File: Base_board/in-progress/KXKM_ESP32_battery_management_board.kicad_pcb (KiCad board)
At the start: 4 copper layers, 56.5 x 57.5 mm, 109 parts, among them J1 Conn_01x06, J11 TEST_1P, J13 Wire pad, J14 Wire pad, J15 Wire pad, J16 Wire pad, J2 TEST_1P, J3 Conn_02x10_Odd_Even, J4 Conn_01x04, J5 Conn_01x02, J6 Conn_01x03, J7 Conn_01x03, J8 Conn_01x03, J9 USB_A, P1 TC_SWD, Q1 BC847W, Q2 BC847W, Q4 2N7002, Q5 2N7002, Q6 2N7002, SW1 SW_Push, SW2 SW_DIP_x03, SW3 SW_Push, SW4 SW_SP3T, U1 ESP32-WROOM, U2 SP3485CN, U3 MCP16331T-E/CH, U4 BTS50080-1TEA, U5 DC_DC_POL, U7 STM32F030F4Px

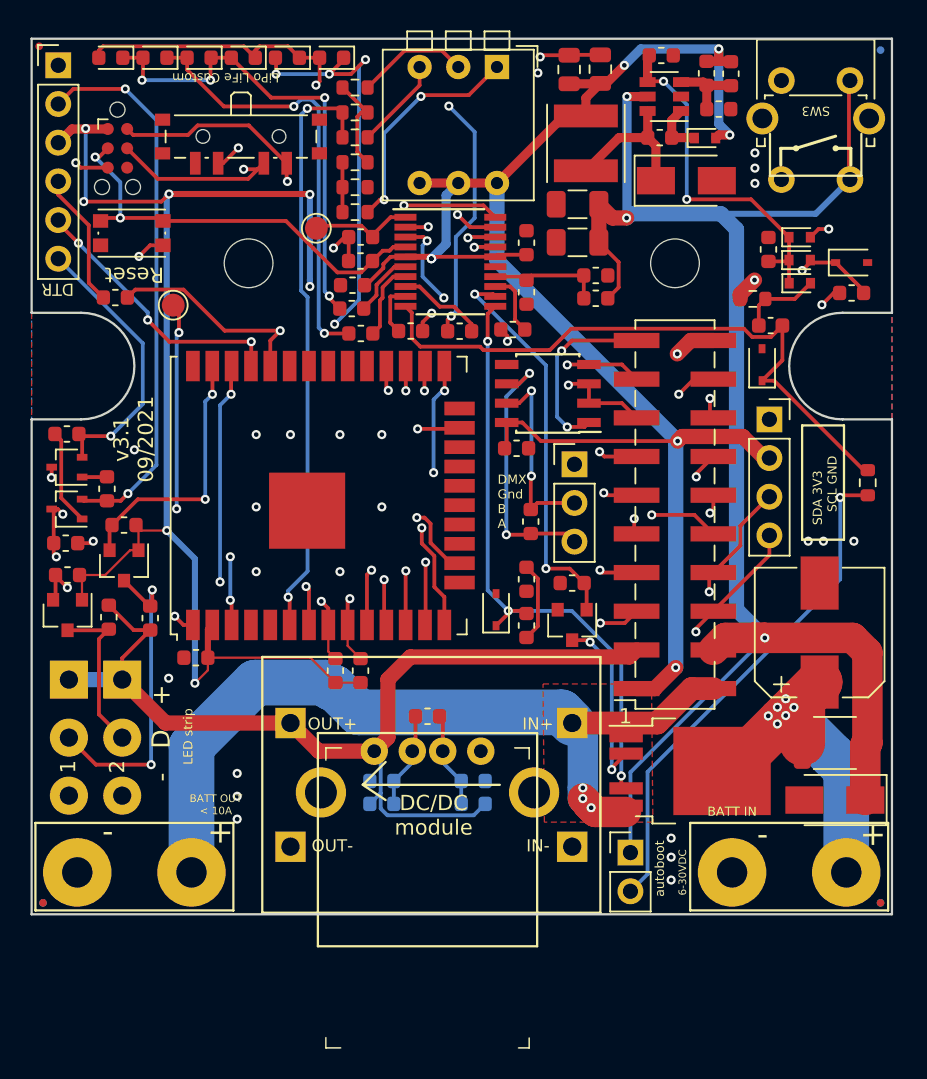
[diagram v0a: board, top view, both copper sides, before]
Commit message: update v3.2
-  connecteur XT60 coudé (et disponible chez JLCPCB)
- modification de l’autoboot pour un redémarrage en cas de perte brêve d’alimentation,
- ajout de l’empreinte pour rajouter une lecteur microSD
- mise à jour des piste de sortie batterie conforme pour 10A
- suppression des pin I2C (déjà dispo sur le GPIO)
- connecteur JST B3B-EH pour un câblage et éviter les soudure qui casse sur les sortie pour LED
- ESP32 en version 16M
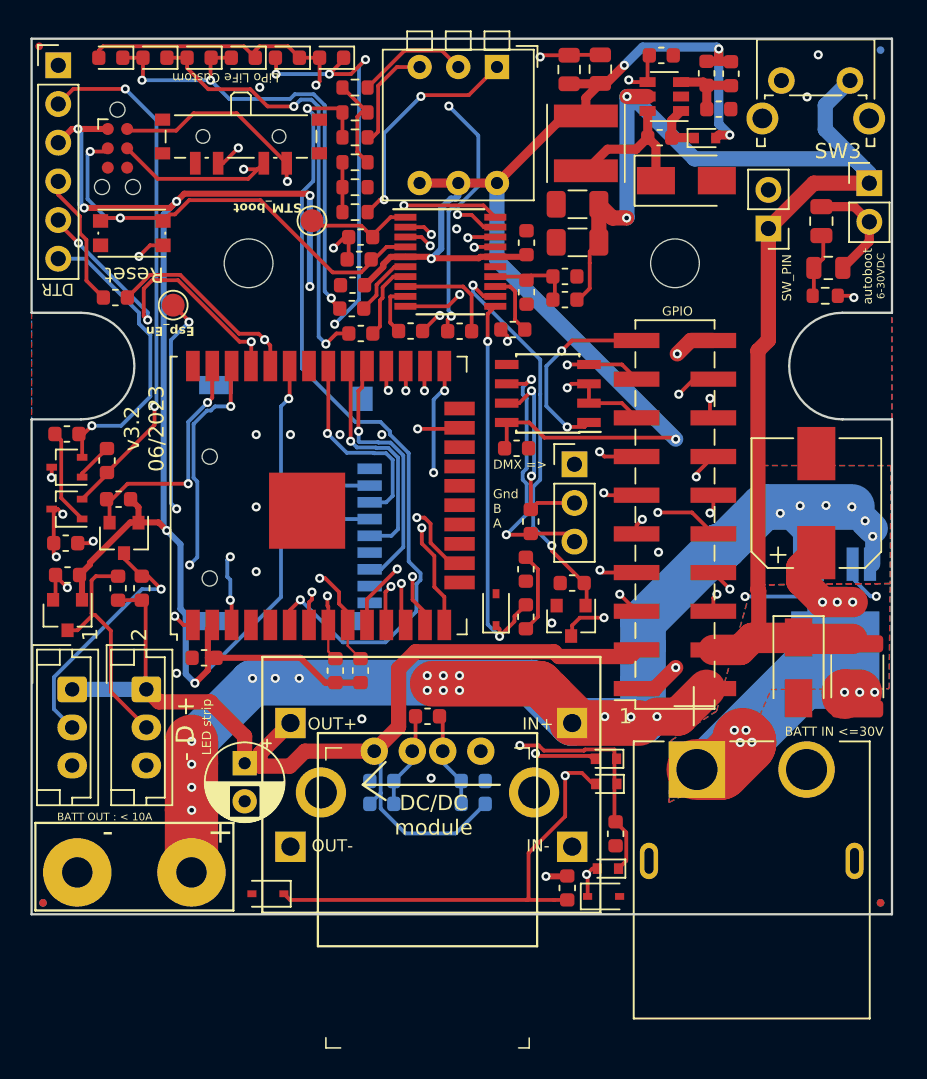
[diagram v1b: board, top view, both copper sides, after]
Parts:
- removed J13, J14: Wire pad, Connector_Wire:SolderWirePad_1x01_Drill2mm
- removed R32: 47k, Resistor_SMD:R_0603_1608Metric
- added C12: 10uF, Capacitor_SMD:C_0805_2012Metric, F.Cu at (154.9, 92.5)
- added C13: 220uF, Capacitor_THT:CP_Radial_D5.0mm_P2.50mm, F.Cu at (117.0, 128.1)
- added J10: XT60PW-M, XT60PW-M:AMASS_XT60PW-M, F.Cu at (150.3, 134.5)
- added J12: Conn_01x02_Socket, Connector_PinHeader_2.54mm:PinHeader_1x02_P2.54mm_Vertical, F.Cu at (151.4, 93.0)
- C11: value 1uF -> 10uF; footprint Capacitor_SMD:C_0603_1608Metric -> Capacitor_SMD:C_0805_2012Metric
- J4: value Conn_01x04 -> 112J-TDAR-R01; footprint Connector_PinSocket_2.54mm:PinSocket_1x04_P2.54mm_Vertical -> KiCad:112JTDARR01; moved to B.Cu
- J7, J8: footprint tom_kicad_lib:SolderWirePad_1x03_P3.81mm_Drill1.2mm -> Connector_JST:JST_EH_B3B-EH-A_1x03_P2.50mm_Vertical
- SW3: footprint tom_kicad_lib:SW_Tactile_SPST_Angled_PTS645Vx58-2LFS_horiz_pads -> Button_Switch_THT:SW_Tactile_SPST_Angled_PTS645Vx31-2LFS
- U4: moved to B.Cu
- U7: value STM32F030F4Px -> STM32F070F6Px
- moved D2 56.5 mm to (118.5, 136.7), turned to 180 degrees
- moved J5 46.7 mm to (158.0, 90.0)
- moved R8 43.3 mm to (138.2, 136.3), turned to -90 degrees
- moved D15 40.5 mm to (140.8, 135.0), turned to 180 degrees
- moved R1 39.7 mm to (141.4, 132.7), turned to -90 degrees
- moved D4 36.7 mm to (140.7, 129.4), turned to 180 degrees
- moved D1 36.5 mm to (140.7, 127.8), turned to 180 degrees
- moved D14 36.4 mm to (140.6, 136.8), turned to 0 degrees
- moved J4 34.0 mm to (117.9, 111.0), turned to 90 degrees
- moved U4 13.4 mm to (155.8, 119.2), turned to -90 degrees
- moved R28 12.6 mm to (155.1, 97.4), turned to 0 degrees
- moved D11 9.00 mm to (153.4, 121.8), turned to -90 degrees
- moved C6 8.50 mm to (154.5, 111.0)
- moved C11 5.36 mm to (155.3, 95.6)
- moved F1 4.62 mm to (157.2, 122.4), turned to -90 degrees
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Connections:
- net /Battery monitoring/STM32_RESET renamed /Battery monitoring/STM32_RST
- net Net-(C26-Pad1) renamed /Power/EN
- C11 pad 1: /Battery monitoring/AUTOBOOT_SENSE -> Net-(J5-Pin_2)
- D15 pad 2: Net-(C11-Pad2) -> /Battery monitoring/AUTOBOOT_SENSE
- J4 pad 1: GND -> unconnected-(J4-DAT2-Pad1)
- J4 pad 2: +3V3 -> /SD_CS
- J4 pad 3: /I2C_SCL -> /SD_DI
- J4 pad 4: /I2C_SDA -> +3V3
- J5 pad 2: Net-(J5-Pad2) -> Net-(J5-Pin_2)
- P1 pad 6: (no net) -> unconnected-(P1-SWO-Pad6)
- R28 pad 1: Net-(J5-Pad2) -> Net-(C11-Pad2)
- SW4 pad 4: (no net) -> unconnected-(SW4-Pad4)
- U1 pad 17: (no net) -> unconnected-(U1-SD2/IO9-Pad17)
- U1 pad 18: (no net) -> unconnected-(U1-SD3/IO10-Pad18)
- U1 pad 19: (no net) -> unconnected-(U1-CMD/IO11-Pad19)
- U1 pad 20: (no net) -> unconnected-(U1-CLK/IO6-Pad20)
- U1 pad 21: (no net) -> unconnected-(U1-SD0/IO7-Pad21)
- U1 pad 22: (no net) -> unconnected-(U1-SD1/IO8-Pad22)
- U1 pad 24: (no net) -> unconnected-(U1-IO2-Pad24)
- U1 pad 29: (no net) -> /SD_DO
- U1 pad 30: (no net) -> /SD_SCK
- U1 pad 31: (no net) -> /SD_DI
- U1 pad 32: (no net) -> unconnected-(U1-NC-Pad32)
- U1 pad 33: (no net) -> /SD_CS
- U1 pad 4: (no net) -> unconnected-(U1-SENSOR_VP-Pad4)
- U1 pad 5: (no net) -> unconnected-(U1-SENSOR_VN-Pad5)
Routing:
- net +VSW: track 96.9 -> 221.3 mm, vias 3 -> 22
- net /Battery monitoring/AUTOBOOT_SENSE: track 41.6 -> 105.5 mm, vias 0 -> 3
- net /Power/EN: track 23.4 -> 80.9 mm
- net Net-(J12-Pin_2): track 20.0 -> 71.3 mm
- net /Battery monitoring/EN_PUSH_BUTTON: track 36.4 -> 71.5 mm, vias 3 -> 2
- net Net-(J5-Pad2): track 33.4 -> 0.00 mm, vias 1 -> 0
- net /Battery monitoring/LOAD_I_SENSE: track 40.7 -> 71.7 mm
- net +BATT_RAW: track 37.6 -> 58.9 mm, vias 6 -> 10
- net +BATT: track 109.0 -> 89.6 mm, vias 3 -> 2
- net /SD_DO: track 0.00 -> 17.4 mm, vias 0 -> 1
- net /SD_SCK: track 0.00 -> 15.3 mm, vias 0 -> 1
- net /Battery monitoring/3.3V_EN: track 29.3 -> 43.8 mm
- net /DIP_SWITCH: track 38.9 -> 53.4 mm
- net /SD_CS: track 0.00 -> 13.5 mm, vias 0 -> 1
- net /SD_DI: track 0.00 -> 13.5 mm, vias 0 -> 1
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- added copper zone on B.Cu, net +BATT_RAW
- added copper zone on F.Cu, net +BATT_RAW
- added copper zone on In1.Cu, net +BATT_RAW
- added copper zone on In2.Cu, net +BATT_RAW
- added copper zone on B.Cu, net +VSW
- added copper zone on In1.Cu, net +VSW
- added copper zone on In2.Cu, net +VSW
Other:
- board text added: "0"
- board text added: "0 mm"
- board text added: "0,01 mm"
- board text added: "0,02"
- board text added: "0,035 mm"
- board text added: "0,1500 mm / 0,0000 mm"
- board text added: "0,3000 mm"
- board text added: "0,48 mm"
- board text added: "1,6000 mm"
- board text added: "2 1"
- board text added: "3,3"
- board text added: "4"
- board text added: "4,5"
- board text added: "56,5000 mm x 57,5000 mm"
- board text added: "B.Cu"
- board text added: "B.Mask"
- board text added: "B.Paste"
- board text added: "B.Silkscreen"
- board text added: "BATT IN <=30V"
- board text added: "BATT OUT : < 10A"
- board text added: "BTS50080-1TEA"
- board text added: "Bottom Silk Screen"
- board text added: "Bottom Solder Mask"
- board text added: "Bottom Solder Paste"
- board text added: "C. Saillant / V. Henry / Tom Magnier v3.2 - 06/2023"
- board text added: "CARACTÉRISTIQUES du PCB"
- board text added: "Connecteurs de bord de cartes:"
- board text added: "Contour du PCB Métallisé:"
- board text added: "Contrôle d'Impédance:"
- board text added: "Couleur"
- board text added: "DMX => Gnd B A"
- board text added: "Diamètre de trou min:"
- board text added: "Dimensions hors tout PCB:"
- board text added: "Diélectrique"
- board text added: "Epaisseur du PCB:"
- board text added: "Epsilon R"
- board text added: "Esp_En"
- board text added: "F.Cu"
- board text added: "F.Mask"
- board text added: "F.Paste"
- board text added: "F.Silkscreen"
- board text added: "FR4"
- board text added: "Finition Cuivre:"
- board text added: "GPIO"
- board text added: "In1.Cu"
- board text added: "In2.Cu"
- board text added: "Matériel"
- board text added: "Micro_SD 112J-TDAR-R01"
- board text added: "Nom de Couche"
- board text added: "Nombre de Couches Cuivre:"
- board text added: "Non"
- board text added: "None"
- board text added: "Not specified"
- board text added: "Pads castellated:"
- board text added: "Piste / espacement min:"
- board text added: "STM_boot"
- board text added: "SW_PIN"
- board text added: "Tg Perte"
- board text added: "Top Silk Screen"
- board text added: "Top Solder Mask"
- board text added: "Top Solder Paste"
- board text added: "Type"
- board text added: "copper"
- board text added: "core"
- board text added: "prepreg"
- board text added: "v3.2 06/2023"
- board text added: "Épaisseur (mm)"
- board text removed: "+ D -"
- board text removed: "BATT IN"
- board text removed: "BATT OUT < 10A"
- board text removed: "DMX Gnd B A"
- board text removed: "IN"
- board text removed: "SDA 3V3 SCL GND"
- board text removed: "SW3"
- board text removed: "V. Henry / Tom Magnier - v3.1 - 09/2021"
- board text removed: "v3.1 09/2021"

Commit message: update to v3.2 and casing 3D View
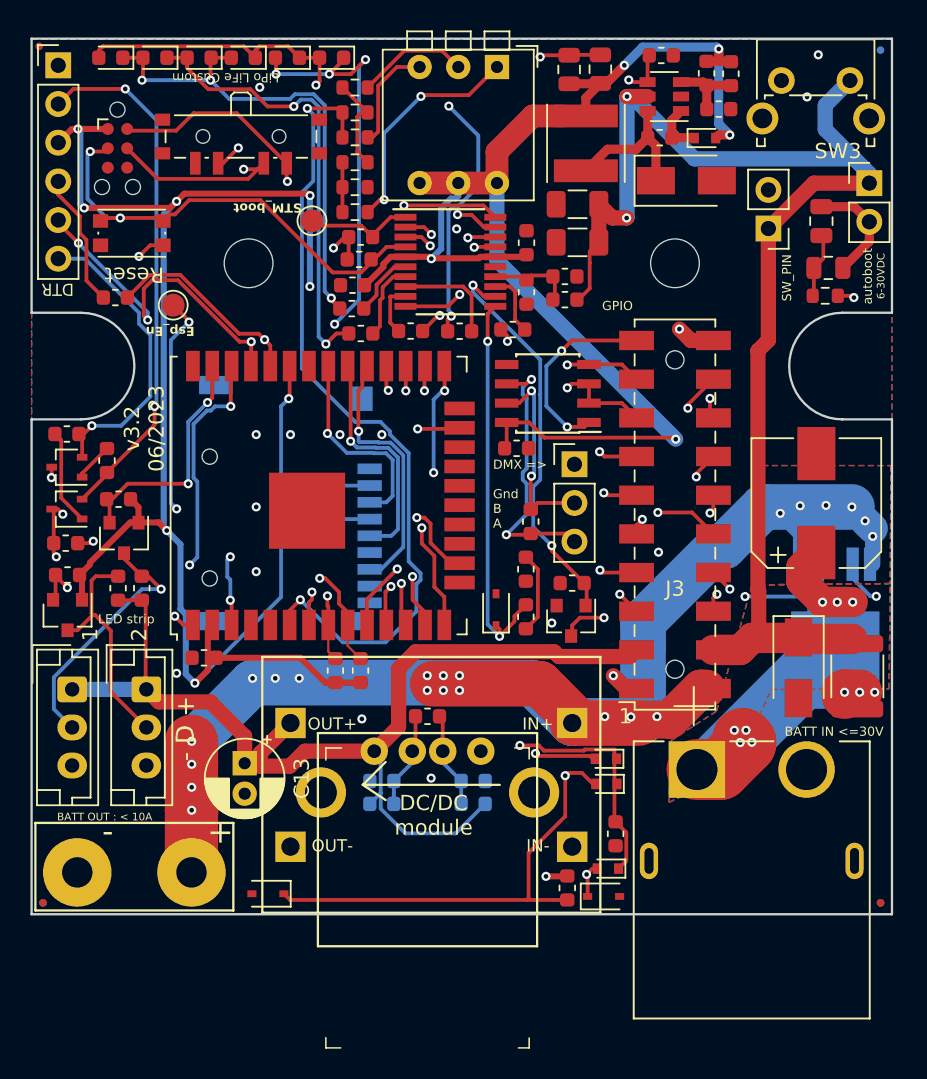
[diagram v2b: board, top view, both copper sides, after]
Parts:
- C13: footprint Capacitor_THT:CP_Radial_D5.0mm_P2.50mm -> Capacitor_THT:CP_Radial_D5.0mm_P2.00mm
- J3: footprint Connector_PinSocket_2.54mm:PinSocket_2x10_P2.54mm_Vertical_SMD -> Connector_Samtec_HLE_SMD:Samtec_HLE-110-02-xxx-DV-LC_2x10_P2.54mm_Horizontal_bis
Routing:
- net +3V3: track 222.9 -> 225.1 mm
- net +VSW: track 221.3 -> 222.7 mm
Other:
- board text added: "0.01 mm"
- board text added: "0.02"
- board text added: "0.034798 mm"
- board text added: "0.1500 mm / 0.1500 mm"
- board text added: "0.3000 mm"
- board text added: "0.48 mm"
- board text added: "1.5992 mm"
- board text added: "3.3"
- board text added: "4.5"
- board text added: "56.5000 mm x 57.5000 mm"
- board text added: "HAL lead-free"
- board text removed: "0,01 mm"
- board text removed: "0,02"
- board text removed: "0,035 mm"
- board text removed: "0,1500 mm / 0,0000 mm"
- board text removed: "0,3000 mm"
- board text removed: "0,48 mm"
- board text removed: "1,6000 mm"
- board text removed: "3,3"
- board text removed: "4,5"
- board text removed: "56,5000 mm x 57,5000 mm"
- board text removed: "None"
